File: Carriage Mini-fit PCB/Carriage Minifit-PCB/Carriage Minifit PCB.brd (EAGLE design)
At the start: 27 x 32 mm, 3 parts, among them J1 39281063, X1 JST-XH-02-PIN-LONG-PAD, X2 TERMINAL-BLOCK-3.5MM-4-PIN-LO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

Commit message: Added Logo
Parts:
- added U$1: FWLOGO_SMALL_FOOTPRINT, FracktalWorks_Eagle_Library:FWLOGO_SMALL
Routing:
- net X_LIM: track 36.1 -> 34.6 mm, vias 0 -> 1
- net CAN_N: track 33.9 -> 35.2 mm
- net CAN_P: track 32.1 -> 33.1 mm
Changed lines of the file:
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@@
 <layer number="56" name="wert" color="7" fill="1" visible="no" active="no"/>
 <layer number="57" name="tCAD" color="7" fill="1" visible="no" active="no"/>
+<layer number="59" name="tCarbon" color="7" fill="1" visible="no" active="no"/>
+<layer number="60" name="bCarbon" color="7" fill="1" visible="no" active="no"/>
 <layer number="88" name="SimResults" color="9" fill="1" visible="no" active="no"/>
 <layer number="89" name="SimProbes" color="9" fill="1" visible="no" active="no"/>
@@
 <layer number="112" name="tSilk" color="7" fill="1" visible="yes" active="yes"/>
 <layer number="113" name="IDFDebug" color="4" fill="1" visible="yes" active="yes"/>
+<layer number="114" name="Badge_Outline" color="7" fill="1" visible="yes" active="yes"/>
+<layer number="115" name="ReferenceISLANDS" color="7" fill="1" visible="yes" active="yes"/>
 <layer number="116" name="Patch_BOT" color="9" fill="4" visible="yes" active="yes"/>
+<layer number="118" name="Rect_Pads" color="7" fill="1" visible="yes" active="yes"/>
 <layer number="121" name="_tsilk" color="7" fill="1" visible="yes" active="yes"/>
 <layer number="122" name="_bsilk" color="7" fill="1" visible="yes" active="yes"/>
@@
 <layer number="127" name="_tValues" color="7" fill="1" visible="yes" active="yes"/>
 <layer number="128" name="_bValues" color="7" fill="1" visible="yes" active="yes"/>
+<layer number="129" name="Mask" color="7" fill="1" visible="yes" active="yes"/>
 <layer number="131" name="tAdjust" color="7" fill="1" visible="yes" active="yes"/>
 <layer number="132" name="bAdjust" color="7" fill="1" visible="yes" active="yes"/>
@@
 <layer number="230" name="230bmp" color="7" fill="1" visible="yes" active="yes"/>
 <layer number="231" name="231bmp" color="7" fill="1" visible="yes" active="yes"/>
+<layer number="232" name="Eagle3D_PG2" color="7" fill="1" visible="yes" active="yes"/>
+<layer number="233" name="Eagle3D_PG3" color="7" fill="1" visible="yes" active="yes"/>
 <layer number="248" name="Housing" color="7" fill="1" visible="yes" active="yes"/>
 <layer number="249" name="Edge" color="7" fill="1" visible="yes" active="yes"/>
@@
 <layer number="251" name="SMDround" color="12" fill="11" visible="no" active="no"/>
 <layer number="254" name="cooling" color="7" fill="1" visible="yes" active="yes"/>
+<layer number="255" name="routoute" color="7" fill="1" visible="yes" active="yes"/>
 </layers>
 <board>
@@
 <attribute name="VALUE" x="20.5717" y="10.1727" size="0.4064" layer="27" rot="R180"/>
 </element>
+<element name="U$1" library="FracktalWorks_Eagle_Library" package="FWLOGO_SMALL" value="FWLOGO_SMALL_FOOTPRINT" x="13.6398" y="15.0114" smashed="yes"/>
 </elements>
 <signals>
@@
 <contactref element="X1" pad="2"/>
 <contactref element="X2" pad="3"/>
-<wire x1="16.3232" y1="25.1324" x2="16.3232" y2="22.0382" width="2.54" layer="1"/>
-<wire x1="11.966" y1="17.681" x2="11.966" y2="5.8912" width="2.54" layer="1"/>
-<wire x1="16.3232" y1="22.0382" x2="11.966" y2="17.681" width="2.54" layer="1"/>
+<wire x1="16.3232" y1="25.1324" x2="16.3232" y2="24.4258" width="2.54" layer="1"/>
+<wire x1="11.966" y1="20.0686" x2="11.966" y2="5.8912" width="2.54" layer="1"/>
+<wire x1="16.3232" y1="24.4258" x2="11.966" y2="20.0686" width="2.54" layer="1"/>
 <wire x1="12.1232" y1="25.1324" x2="16.3232" y2="25.1324" width="1.016" layer="1"/>
-<wire x1="11.966" y1="5.8912" x2="11.966" y2="4.1376" width="1.016" layer="16"/>
-<wire x1="13.0391375" y1="3.0644625" x2="25.6794" y2="3.0644625" width="1.016" layer="16"/>
-<wire x1="25.6794" y1="3.0644625" x2="26.3398" y2="3.7248625" width="1.016" layer="16"/>
-<wire x1="26.3398" y1="3.7248625" x2="26.3398" y2="5.3594" width="1.016" layer="16"/>
-<wire x1="11.966" y1="4.1376" x2="13.0391375" y2="3.0644625" width="1.016" layer="16"/>
+<wire x1="26.3398" y1="5.3594" x2="26.3398" y2="3.7846" width="0.6096" layer="16"/>
+<wire x1="26.3398" y1="3.7846" x2="25.6286" y2="3.0734" width="0.6096" layer="16"/>
+<wire x1="25.6286" y1="3.0734" x2="12.7254" y2="3.0734" width="0.6096" layer="16"/>
+<wire x1="11.966" y1="3.8328" x2="11.966" y2="5.8912" width="0.6096" layer="16"/>
+<wire x1="12.7254" y1="3.0734" x2="11.966" y2="3.8328" width="0.6096" layer="16"/>
 </signal>
 <signal name="X_LIM">
 <contactref element="J1" pad="3"/>
 <contactref element="X1" pad="1"/>
-<wire x1="12.1232" y1="30.6324" x2="9.7536" y2="28.2628" width="1.016" layer="16"/>
-<wire x1="9.7536" y1="28.2628" x2="9.7536" y2="13.5128" width="1.016" layer="16"/>
-<wire x1="9.7536" y1="13.5128" x2="12.0904" y2="11.176" width="1.016" layer="16"/>
-<wire x1="23.7998" y1="6.2992" x2="23.7998" y2="5.3594" width="1.016" layer="16"/>
-<wire x1="12.0904" y1="11.176" x2="18.923" y2="11.176" width="1.016" layer="16"/>
-<wire x1="18.923" y1="11.176" x2="23.7998" y2="6.2992" width="1.016" layer="16"/>
+<wire x1="12.1232" y1="30.6324" x2="9.525" y2="28.0342" width="0.6096" layer="16"/>
+<wire x1="9.525" y1="16.4084" x2="14.7066" y2="11.2268" width="0.6096" layer="16"/>
+<via x="14.7066" y="11.2268" extent="1-16" drill="0.35"/>
+<wire x1="14.7066" y1="11.2268" x2="18.6944" y2="11.2268" width="0.6096" layer="1"/>
+<wire x1="23.7998" y1="6.1214" x2="23.7998" y2="5.3594" width="0.6096" layer="1"/>
+<wire x1="9.525" y1="28.0342" x2="9.525" y2="16.4084" width="0.6096" layer="16"/>
+<wire x1="18.6944" y1="11.2268" x2="23.7998" y2="6.1214" width="0.6096" layer="1"/>
 </signal>
 <signal name="CAN_P" class="1">
 <contactref element="J1" pad="4"/>
 <contactref element="X2" pad="2"/>
-<wire x1="15.466" y1="5.8912" x2="16.6064" y2="7.0316" width="1.016" layer="1"/>
-<wire x1="16.6064" y1="18.1326125" x2="19.8351875" y2="21.3614" width="1.016" layer="1"/>
-<wire x1="19.8351875" y1="21.3614" x2="23.4696" y2="21.3614" width="1.016" layer="1"/>
-<wire x1="23.4696" y1="21.3614" x2="24.5618" y2="22.4536" width="1.016" layer="1"/>
-<wire x1="22.5298" y1="27.4066" x2="21.2598" y2="27.4066" width="1.016" layer="1"/>
-<wire x1="20.5232" y1="26.67" x2="20.5232" y2="25.1324" width="1.016" layer="1"/>
-<wire x1="21.2598" y1="27.4066" x2="20.5232" y2="26.67" width="1.016" layer="1"/>
-<wire x1="16.6064" y1="7.0316" x2="16.6064" y2="18.1326125" width="1.016" layer="1"/>
-<wire x1="24.5618" y1="22.4536" x2="24.5618" y2="25.3746" width="1.016" layer="1"/>
-<wire x1="24.5618" y1="25.3746" x2="22.5298" y2="27.4066" width="1.016" layer="1"/>
+<wire x1="15.466" y1="5.8912" x2="16.6064" y2="7.0316" width="1.016" layer="16"/>
+<wire x1="16.6064" y1="19.3772125" x2="18.6413875" y2="21.4122" width="1.016" layer="16"/>
+<wire x1="18.6413875" y1="21.4122" x2="24.1808" y2="21.4122" width="1.016" layer="16"/>
+<wire x1="24.1808" y1="21.4122" x2="24.3332" y2="21.5646" width="1.016" layer="16"/>
+<wire x1="24.3332" y1="21.5646" x2="24.3332" y2="25.781" width="1.016" layer="16"/>
+<wire x1="24.3332" y1="25.781" x2="22.86" y2="27.2542" width="1.016" layer="16"/>
+<wire x1="22.86" y1="27.2542" x2="20.8788" y2="27.2542" width="1.016" layer="16"/>
+<wire x1="20.5232" y1="26.8986" x2="20.5232" y2="25.1324" width="1.016" layer="16"/>
+<wire x1="20.8788" y1="27.2542" x2="20.5232" y2="26.8986" width="1.016" layer="16"/>
+<wire x1="16.6064" y1="7.0316" x2="16.6064" y2="19.3772125" width="1.016" layer="16"/>
 </signal>
 <signal name="CAN_N" class="1">
 <contactref element="J1" pad="1"/>
 <contactref element="X2" pad="1"/>
-<wire x1="18.966" y1="5.8912" x2="17.8256" y2="7.0316" width="1.016" layer="1"/>
-<wire x1="17.8256" y1="7.0316" x2="17.8256" y2="17.6276" width="1.016" layer="1"/>
-<wire x1="17.8256" y1="17.6276" x2="20.3402" y2="20.1422" width="1.016" layer="1"/>
-<wire x1="23.9746125" y1="20.1422" x2="25.781" y2="21.9485875" width="1.016" layer="1"/>
-<wire x1="23.0348125" y1="28.6258" x2="21.2598" y2="28.6258" width="1.016" layer="1"/>
-<wire x1="20.5232" y1="29.3624" x2="20.5232" y2="30.6324" width="1.016" layer="1"/>
-<wire x1="21.2598" y1="28.6258" x2="20.5232" y2="29.3624" width="1.016" layer="1"/>
-<wire x1="20.3402" y1="20.1422" x2="23.9746125" y2="20.1422" width="1.016" layer="1"/>
-<wire x1="25.781" y1="21.9485875" x2="25.781" y2="25.8796125" width="1.016" layer="1"/>
-<wire x1="25.781" y1="25.8796125" x2="23.0348125" y2="28.6258" width="1.016" layer="1"/>
+<wire x1="18.966" y1="5.8912" x2="17.8256" y2="7.0316" width="1.016" layer="16"/>
+<wire x1="17.8256" y1="7.0316" x2="17.8256" y2="18.8722" width="1.016" layer="16"/>
+<wire x1="17.8256" y1="18.8722" x2="19.1464" y2="20.193" width="1.016" layer="16"/>
+<wire x1="24.6858125" y1="20.193" x2="25.5524" y2="21.0595875" width="1.016" layer="16"/>
+<wire x1="25.5524" y1="26.2860125" x2="23.3650125" y2="28.4734" width="1.016" layer="16"/>
+<wire x1="23.3650125" y1="28.4734" x2="20.8788" y2="28.4734" width="1.016" layer="16"/>
+<wire x1="20.5232" y1="28.829" x2="20.5232" y2="30.6324" width="1.016" layer="16"/>
+<wire x1="20.8788" y1="28.4734" x2="20.5232" y2="28.829" width="1.016" layer="16"/>
+<wire x1="19.1464" y1="20.193" x2="24.6858125" y2="20.193" width="1.016" layer="16"/>
+<wire x1="25.5524" y1="21.0595875" x2="25.5524" y2="26.2860125" width="1.016" layer="16"/>
 </signal>
 </signals>

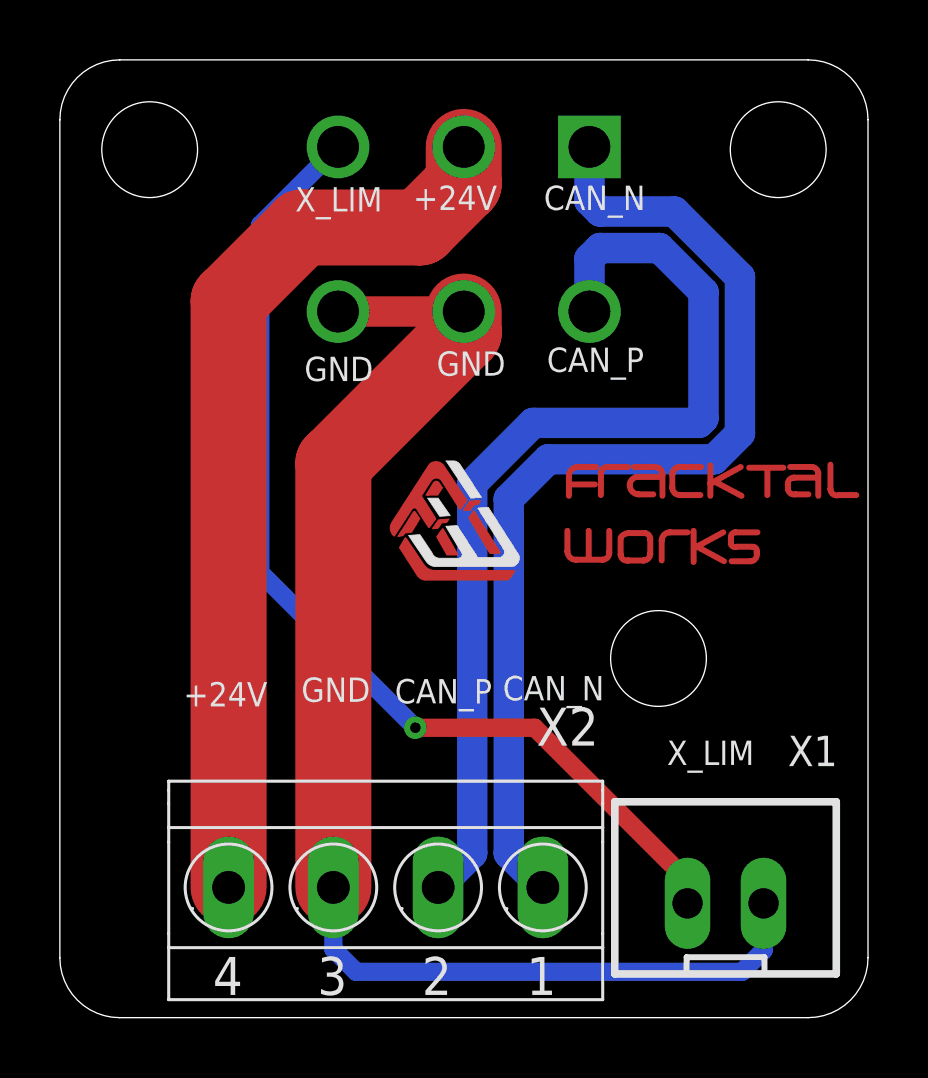
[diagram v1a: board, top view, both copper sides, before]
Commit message: Updated Toolboard V2 and Carriage minifit boards specs
Toolboard and Carriage minifit board design,  gerber, BOMs, centroids and connector specifications have been updated here
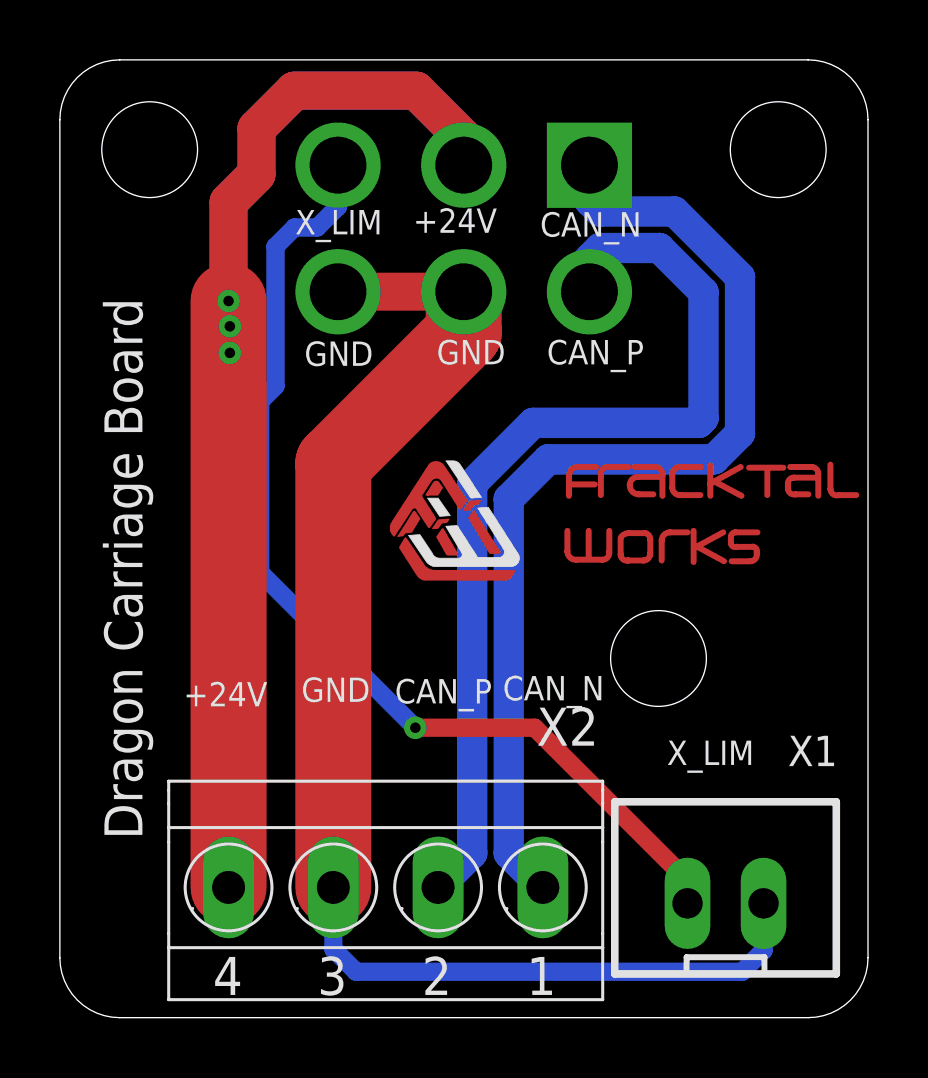
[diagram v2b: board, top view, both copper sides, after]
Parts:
- removed J1: 39281063, Minifit Jr 2x3:MOLEX_39281063
- added U$2: 6P_2X3_MINIFIT_JR_4.2MM_MALE, 6P_2x3_Minifit_Jr_4.2mm_Male:6P_2X3_MINIFIT_JR_4.2MM_MALE
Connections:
- net +24V: now also U$2.2; no longer J1.2
- net CAN_N: now also U$2.1; no longer J1.1
- net CAN_P: now also U$2.4; no longer J1.4
- net GND: now also U$2.5, U$2.6; no longer J1.5, J1.6
- net X_LIM: now also U$2.3; no longer J1.3
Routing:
- net +24V: track 30.3 -> 51.7 mm, vias 0 -> 3
- net GND: track 43.9 -> 44.5 mm
- net CAN_P: track 33.1 -> 32.5 mm
- net CAN_N: track 35.2 -> 34.6 mm
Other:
- board text added: "Dragon Carriage Board"
